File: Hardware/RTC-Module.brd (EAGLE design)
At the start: 25.4 x 25.4 mm, 18 parts, among them J4 455-1750-1-ND

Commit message: Board ready for design review
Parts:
- removed U$2: LOGO-SFESK, SparkFun:SFE-LOGO-FLAME
- added FD1, FD2, FD3, FD4: FIDUCIALUFIDUCIAL, SparkFun-Aesthetics:FIDUCIAL-MICRO
- added LOGO2: SFE_LOGO_FLAME.1_INCH, SparkFun-Aesthetics:SFE_LOGO_FLAME_.1
- added LOGO3: SFE_LOGO_NAME_FLAME.1_INCH, SparkFun-Aesthetics:SFE_LOGO_NAME_FLAME_.1
- BAT1: device SparkFun-Electromechanical:BATTCON_12MM_PTH -> SparkFun-Batteries:BATTCON_12MM_PTH
- moved FRAME2 67.9 mm to (-12.7, -8.89)
- moved LOGO1 37.9 mm to (2.54, 18.2)
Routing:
- net SDA: track 22.6 -> 48.6 mm, vias 0 -> 2
- net SCL: track 17.3 -> 40.6 mm, vias 2 -> 3
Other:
- board text added: "Andy England"
- board text added: "v01"
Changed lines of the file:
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@@
 <text x="17.907" y="9.779" size="0.8128" layer="21" font="vector" ratio="15" rot="R180" align="center">I</text>
 <text x="16.383" y="9.779" size="0.8128" layer="21" font="vector" ratio="15" rot="R180" align="center">F</text>
+<text x="24.892" y="0.508" size="1.27" layer="16" font="vector" ratio="15" rot="MR0">v01</text>
+<text x="13.97" y="-8.89" size="1.778" layer="51">Andy England</text>
 </plain>
 <attributes>
@@
 </autorouter>
 <elements>
-<element name="BAT1" library="SparkFun-Electromechanical" package="BATTCON_12MM_PTH" value="" x="12.7" y="19.05"/>
+<element name="BAT1" library="SparkFun-Batteries" package="BATTCON_12MM_PTH" value="" x="12.7" y="19.05">
+<attribute name="SF_SKU" value="PRT-07948" x="12.7" y="19.05" size="1.778" layer="27" display="off"/>
+<attribute name="PROD_ID" value="BATT-08315" x="12.7" y="19.05" size="1.778" layer="27" display="off"/>
+</element>
 <element name="C1" library="SparkFun-Capacitors" package="0603-CAP" value="0.1uF" x="22.86" y="7.62" rot="R270">
 <attribute name="PROD_ID" value="CAP-00810" x="22.86" y="7.62" size="1.778" layer="27" rot="R270" display="off"/>
 </element>
-<element name="FRAME2" library="SparkFun-Aesthetics" package="CREATIVE_COMMONS" value="FRAME-LETTER" x="-76.2" y="15.24"/>
+<element name="FRAME2" library="SparkFun-Aesthetics" package="CREATIVE_COMMONS" value="FRAME-LETTER" x="-12.7" y="-8.89"/>
 <element name="J1" library="SparkFun-Connectors" package="1X04_1MM_RA" value="" x="5.08" y="12.7" rot="R270">
 <attribute name="PROD_ID" value="CONN-13694" x="5.08" y="12.7" size="1.778" layer="27" rot="R270" display="off"/>
@@
 <attribute name="PROD_ID" value="XXX-00000" x="15.24" y="1.27" size="1.778" layer="27" display="off"/>
 </element>
-<element name="LOGO1" library="SparkFun-Aesthetics" package="OSHW-LOGO-S" value="OSHW-LOGOS" x="-30.48" y="36.83"/>
+<element name="LOGO1" library="SparkFun-Aesthetics" package="OSHW-LOGO-S" value="OSHW-LOGOS" x="2.54" y="18.161"/>
 <element name="R1" library="SparkFun-Resistors" package="0603" value="4.7k" x="7.62" y="7.62" rot="R90">
 <attribute name="PROD_ID" value="RES-07857" x="7.62" y="7.62" size="1.778" layer="27" rot="R90" display="off"/>
@@
 <element name="SJ1" library="SparkFun-Passives" package="SJ_3_PASTE1&amp;2&amp;3" value="" x="17.145" y="11.43"/>
 <element name="SJ2" library="SparkFun-Passives" package="SJ_3_PASTE1&amp;2&amp;3" value="" x="8.255" y="11.43"/>
-<element name="U$2" library="SparkFun" package="SFE-LOGO-FLAME" value="LOGO-SFESK" x="-24.13" y="31.75"/>
 <element name="U$6" library="SparkFun" package="STAND-OFF" value="STAND-OFF" x="22.86" y="22.86" rot="R180"/>
 <element name="U$7" library="SparkFun" package="STAND-OFF" value="STAND-OFF" x="2.54" y="22.86" rot="R180"/>
+<element name="LOGO2" library="SparkFun-Aesthetics" package="SFE_LOGO_FLAME_.1" value="SFE_LOGO_FLAME.1_INCH" x="21.717" y="16.764"/>
+<element name="LOGO3" library="SparkFun-Aesthetics" package="SFE_LOGO_NAME_FLAME_.1" value="SFE_LOGO_NAME_FLAME.1_INCH" x="18.669" y="13.843" rot="MR0"/>
+<element name="FD1" library="SparkFun-Aesthetics" package="FIDUCIAL-MICRO" value="FIDUCIALUFIDUCIAL" x="24.13" y="17.78" rot="MR0"/>
+<element name="FD2" library="SparkFun-Aesthetics" package="FIDUCIAL-MICRO" value="FIDUCIALUFIDUCIAL" x="24.13" y="17.78"/>
+<element name="FD3" library="SparkFun-Aesthetics" package="FIDUCIAL-MICRO" value="FIDUCIALUFIDUCIAL" x="1.27" y="1.27" rot="MR0"/>
+<element name="FD4" library="SparkFun-Aesthetics" package="FIDUCIAL-MICRO" value="FIDUCIALUFIDUCIAL" x="1.27" y="1.27"/>
 </elements>
 <signals>
@@
 <via x="19.05" y="10.668" extent="1-16" drill="0.381"/>
 <via x="22.86" y="5.588" extent="1-16" drill="0.381"/>
+<via x="16.129" y="8.763" extent="1-16" drill="0.381"/>
+<via x="16.51" y="4.064" extent="1-16" drill="0.381"/>
+<via x="19.05" y="5.334" extent="1-16" drill="0.381"/>
+<via x="13.97" y="2.667" extent="1-16" drill="0.381"/>
 </signal>
 <signal name="SCL">
@@
 <wire x1="3.81" y1="10.795" x2="4.215" y2="11.2" width="0.2032" layer="1"/>
 <wire x1="4.215" y1="11.2" x2="5.08" y2="11.2" width="0.2032" layer="1"/>
-<wire x1="11.43" y1="3.81" x2="20.32" y2="14.2" width="0" layer="19" extent="1-1"/>
+<wire x1="12.7" y1="1.27" x2="12.7" y2="2.54" width="0.2032" layer="16"/>
+<wire x1="12.7" y1="2.54" x2="21.59" y2="11.43" width="0.2032" layer="16"/>
+<wire x1="21.59" y1="11.43" x2="22.86" y2="11.43" width="0.2032" layer="16"/>
+<wire x1="22.86" y1="11.43" x2="24.13" y2="12.7" width="0.2032" layer="16"/>
+<wire x1="24.13" y1="12.7" x2="24.13" y2="13.97" width="0.2032" layer="16"/>
+<wire x1="24.13" y1="13.97" x2="22.86" y2="15.24" width="0.2032" layer="16"/>
+<wire x1="22.86" y1="15.24" x2="21.59" y2="15.24" width="0.2032" layer="16"/>
+<via x="21.59" y="15.24" extent="1-16" drill="0.381"/>
+<wire x1="21.59" y1="15.24" x2="20.828" y2="15.24" width="0.2032" layer="1"/>
+<wire x1="20.828" y1="15.24" x2="20.32" y2="14.732" width="0.2032" layer="1"/>
+<wire x1="20.32" y1="14.732" x2="20.32" y2="14.2" width="0.2032" layer="1"/>
 </signal>
 <signal name="SDA">
@@
 <wire x1="10.16" y1="1.27" x2="10.16" y2="2.54" width="0.2032" layer="1"/>
 <wire x1="10.16" y1="2.54" x2="9.398" y2="3.302" width="0.2032" layer="1"/>
-<wire x1="5.08" y1="12.2" x2="3.31" y2="12.2" width="0.2032" layer="1"/>
-<wire x1="3.31" y1="12.2" x2="2.921" y2="11.811" width="0.2032" layer="1"/>
-<wire x1="2.921" y1="11.811" x2="2.921" y2="4.191" width="0.2032" layer="1"/>
+<wire x1="5.08" y1="12.2" x2="2.921" y2="12.2" width="0.2032" layer="1"/>
+<wire x1="2.921" y1="12.2" x2="2.532" y2="12.2" width="0.2032" layer="1"/>
+<wire x1="2.921" y1="12.2" x2="2.921" y2="4.191" width="0.2032" layer="1"/>
 <wire x1="2.921" y1="4.191" x2="3.81" y2="3.302" width="0.2032" layer="1"/>
-<wire x1="5.08" y1="6.77" x2="5.08" y2="3.81" width="0.2032" layer="1"/>
+<wire x1="5.08" y1="6.77" x2="5.08" y2="3.302" width="0.2032" layer="1"/>
 <wire x1="5.08" y1="3.302" x2="3.81" y2="3.302" width="0.2032" layer="1"/>
 <wire x1="9.398" y1="3.302" x2="5.08" y2="3.302" width="0.2032" layer="1"/>
-<wire x1="5.08" y1="3.302" x2="5.08" y2="3.81" width="0.2032" layer="1"/>
-<wire x1="10.16" y1="2.54" x2="20.32" y2="13.2" width="0" layer="19" extent="1-1"/>
+<via x="2.032" y="12.7" extent="1-16" drill="0.381"/>
+<wire x1="2.032" y1="12.7" x2="2.532" y2="12.2" width="0.2032" layer="1"/>
+<wire x1="2.032" y1="12.7" x2="11.43" y2="12.7" width="0.2032" layer="16"/>
+<wire x1="11.43" y1="12.7" x2="12.7" y2="13.97" width="0.2032" layer="16"/>
+<wire x1="12.7" y1="13.97" x2="21.59" y2="13.97" width="0.2032" layer="16"/>
+<wire x1="20.32" y1="13.2" x2="22.36" y2="13.2" width="0.2032" layer="1"/>
+<wire x1="22.36" y1="13.2" x2="22.86" y2="12.7" width="0.2032" layer="1"/>
+<via x="22.86" y="12.7" extent="1-16" drill="0.381"/>
+<wire x1="22.86" y1="12.7" x2="21.59" y2="13.97" width="0.2032" layer="16"/>
 </signal>
 <signal name="N$5">

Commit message: post design review changes
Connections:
- net SCL: now also RTC1.8
- net SDA: now also RTC1.7
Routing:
- net SCL: track 40.6 -> 56.8 mm, vias 3 -> 4
- net SDA: track 48.6 -> 50.2 mm, vias 2 -> 3
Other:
- board text added: "0xD0"
- board text added: "32KHZ"
- board text added: "Qwiic RTC Module"
- board text added: "SQW/!INT"
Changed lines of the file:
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@@
 <layer number="45" name="Holes" color="7" fill="1" visible="no" active="yes"/>
 <layer number="46" name="Milling" color="3" fill="1" visible="no" active="yes"/>
-<layer number="47" name="Measures" color="7" fill="1" visible="no" active="yes"/>
+<layer number="47" name="Measures" color="7" fill="1" visible="yes" active="yes"/>
 <layer number="48" name="Document" color="7" fill="1" visible="yes" active="yes"/>
 <layer number="49" name="Reference" color="7" fill="1" visible="yes" active="yes"/>
@@
 <text x="12.7" y="3.937" size="0.8128" layer="22" font="vector" ratio="15" rot="MR270" align="center">SCL</text>
 <text x="15.24" y="3.937" size="0.8128" layer="22" font="vector" ratio="15" rot="MR270" align="center">!RST</text>
-<text x="17.78" y="3.937" size="0.8128" layer="22" font="vector" ratio="15" rot="MR270" align="center">!INT</text>
-<text x="20.32" y="3.937" size="0.8128" layer="22" font="vector" ratio="15" rot="MR270" align="center">32K</text>
+<text x="17.78" y="5.207" size="0.8128" layer="22" font="vector" ratio="15" rot="MR270" align="center">SQW/!INT</text>
+<text x="20.32" y="4.699" size="0.8128" layer="22" font="vector" ratio="15" rot="MR270" align="center">32KHZ</text>
 <text x="8.382" y="9.779" size="0.8128" layer="21" font="vector" ratio="15" rot="R180" align="center">I2C</text>
 <text x="17.907" y="9.779" size="0.8128" layer="21" font="vector" ratio="15" rot="R180" align="center">I</text>
 <text x="16.383" y="9.779" size="0.8128" layer="21" font="vector" ratio="15" rot="R180" align="center">F</text>
 <text x="24.892" y="0.508" size="1.27" layer="16" font="vector" ratio="15" rot="MR0">v01</text>
-<text x="13.97" y="-8.89" size="1.778" layer="51">Andy England</text>
+<text x="17.78" y="-8.89" size="1.778" layer="51">Andy England</text>
+<text x="12.7" y="10.795" size="1.27" layer="22" font="vector" ratio="15" rot="MR0" align="center">Qwiic RTC
+Module</text>
+<text x="12.7" y="7.62" size="1.016" layer="22" font="vector" ratio="15" rot="MR0" align="center">0xD0</text>
+<dimension x1="0" y1="25.4" x2="0" y2="0" x3="-7.62" y3="12.7" textsize="1.016" textratio="15" layer="47" unit="inch"/>
+<dimension x1="2.54" y1="22.86" x2="2.54" y2="0" x3="-3.81" y3="11.43" textsize="1.016" textratio="15" layer="47" unit="inch"/>
+<dimension x1="2.54" y1="22.86" x2="22.86" y2="22.86" x3="12.7" y3="26.67" textsize="1.016" textratio="15" layer="47" unit="inch"/>
+<dimension x1="25.4" y1="25.4" x2="0" y2="25.4" x3="12.7" y3="30.48" textsize="1.016" textratio="15" layer="47" unit="inch"/>
 </plain>
 <attributes>
@@
 <vertex x="25.4" y="0"/>
 </polygon>
-<via x="1.27" y="11.43" extent="1-16" drill="0.381"/>
+<via x="1.27" y="11.303" extent="1-16" drill="0.381"/>
 <via x="1.27" y="8.382" extent="1-16" drill="0.381"/>
 <via x="19.05" y="10.668" extent="1-16" drill="0.381"/>
@@
 <wire x1="20.828" y1="15.24" x2="20.32" y2="14.732" width="0.2032" layer="1"/>
 <wire x1="20.32" y1="14.732" x2="20.32" y2="14.2" width="0.2032" layer="1"/>
+<contactref element="RTC1" pad="8"/>
+<wire x1="10.795" y1="11.69" x2="10.795" y2="13.335" width="0.2032" layer="1"/>
+<wire x1="10.795" y1="13.335" x2="10.16" y2="13.97" width="0.2032" layer="1"/>
+<via x="10.16" y="13.97" extent="1-16" drill="0.381"/>
+<wire x1="10.16" y1="13.97" x2="1.778" y2="13.97" width="0.2032" layer="16"/>
+<wire x1="1.778" y1="13.97" x2="1.143" y2="13.335" width="0.2032" layer="16"/>
+<wire x1="1.143" y1="13.335" x2="1.143" y2="12.446" width="0.2032" layer="16"/>
+<wire x1="1.143" y1="12.446" x2="1.651" y2="11.938" width="0.2032" layer="16"/>
+<wire x1="1.651" y1="11.938" x2="2.286" y2="11.938" width="0.2032" layer="16"/>
+<wire x1="2.286" y1="11.938" x2="3.81" y2="10.414" width="0.2032" layer="16"/>
 </signal>
 <signal name="SDA">
@@
 <wire x1="2.032" y1="12.7" x2="2.532" y2="12.2" width="0.2032" layer="1"/>
 <wire x1="2.032" y1="12.7" x2="11.43" y2="12.7" width="0.2032" layer="16"/>
-<wire x1="11.43" y1="12.7" x2="12.7" y2="13.97" width="0.2032" layer="16"/>
+<wire x1="11.43" y1="12.7" x2="12.065" y2="13.335" width="0.2032" layer="16"/>
+<wire x1="12.065" y1="13.335" x2="12.7" y2="13.97" width="0.2032" layer="16"/>
 <wire x1="12.7" y1="13.97" x2="21.59" y2="13.97" width="0.2032" layer="16"/>
 <wire x1="20.32" y1="13.2" x2="22.36" y2="13.2" width="0.2032" layer="1"/>
@@
 <via x="22.86" y="12.7" extent="1-16" drill="0.381"/>
 <wire x1="22.86" y1="12.7" x2="21.59" y2="13.97" width="0.2032" layer="16"/>
+<contactref element="RTC1" pad="7"/>
+<wire x1="12.065" y1="11.69" x2="12.065" y2="13.335" width="0.2032" layer="1"/>
+<via x="12.065" y="13.335" extent="1-16" drill="0.381"/>
 </signal>
 <signal name="N$5">
@@
 </board>
 </drawing>
+<compatibility>
+<note version="6.3" minversion="6.2.2" severity="warning">
+Since Version 6.2.2 text objects can contain more than one line,
+which will not be processed correctly with this version.
+</note>
+</compatibility>
 </eagle>

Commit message: updated sensor
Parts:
- removed R4: 4.7k, SparkFun-Resistors:0603
- removed RTC1: DS3231M, SparkFun-Clocks:SO08
- removed SJ1: (no value), SparkFun-Passives:SJ_3_PASTE1&2&3
- added C2: 10nF, SparkFun-Capacitors:0603
- added D1: 0.5A/40V/420mV, SparkFun-DiscreteSemi:SOD-323
- added D2: 120mA/40V/370mV, SparkFun-DiscreteSemi:SOD-523
- added JP1: JUMPER-SMT_2_NC_PASTE_SILK, SparkFun-Jumpers:SMT-JUMPER_2_NC_PASTE_SILK
- added R5: 1k, SparkFun-Resistors:0603
- added U1: RV-4162-C7, SparkFun-Clocks:RV-4162-C7-SMT
- C1: value 0.1uF -> 1.0uF; device SparkFun-Capacitors:0603-CAP -> SparkFun-Capacitors:0603
- J3: device SparkFun-Connectors:1X04 -> SparkFun-Connectors:1X04_NO_SILK
- J4: value 455-1750-1-ND -> (none); device SparkFun-Connectors:1X03 -> SparkFun-Connectors:1X01_NO_SILK
- R1, R2, R3: device SparkFun-Resistors:0603 -> SparkFun-Resistors:0603@1
- moved C1 8.03 mm to (15.2, 5.08), turned to 0 degrees
- moved R3 2.74 mm to (17.8, 8.64)
- moved J4 2.54 mm to (17.8, 1.27)
- moved J3 2.54 mm to (7.62, 1.27)
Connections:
- removed net !INT/SQW: J4.2, R4.1, RTC1.3
- removed net !RST: J4.1, RTC1.4
- removed net 32KHZ: J4.3, R3.1, RTC1.1
- removed net N$1: BAT1.VCC@1, RTC1.6
- removed net N$3: R4.2, SJ1.1
- new net !INT: J4.1, R3.1, U1.6
- new net BATTERY: BAT1.VCC@1, C1.1, D2.A, R5.1
- new net CLKOUT: U1.2
- new net N$4: D1.C, R5.2
- net 3.3V: now also C2.1, D1.A, D2.C, JP1.2, U1.5; no longer C1.1, RTC1.2, SJ1.2
- net GND: now also C2.2, U1.3; no longer RTC1.5
- net N$2: now also JP1.1; no longer SJ1.3
- net SCL: now also U1.8; no longer RTC1.8
- net SDA: now also U1.1; no longer RTC1.7
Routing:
- net SCL: track 56.8 -> 0.00 mm, vias 4 -> 0
- net SDA: track 50.2 -> 0.00 mm, vias 3 -> 0
- net 3.3V: track 41.7 -> 4.65 mm, vias 3 -> 0
- net 32KHZ: track 16.8 -> 0.00 mm
- net N$1: track 12.1 -> 0.00 mm
- net !INT/SQW: track 11.0 -> 0.00 mm
- net BATTERY: track 0.00 -> 10.4 mm
- net !RST: track 5.08 -> 0.00 mm
- net N$2: track 4.83 -> 0.00 mm
- net N$3: track 4.08 -> 0.00 mm
- net N$5: track 6.03 -> 3.93 mm
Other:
- board text removed: "!INT"
- board text removed: "!RST"
- board text removed: "0xD0"
- board text removed: "3.3V"
- board text removed: "32K"
- board text removed: "32KHZ"
- board text removed: "F"
- board text removed: "GND"
- board text removed: "I"
- board text removed: "SCL"
- board text removed: "SDA"
- board text removed: "SQW/!INT"

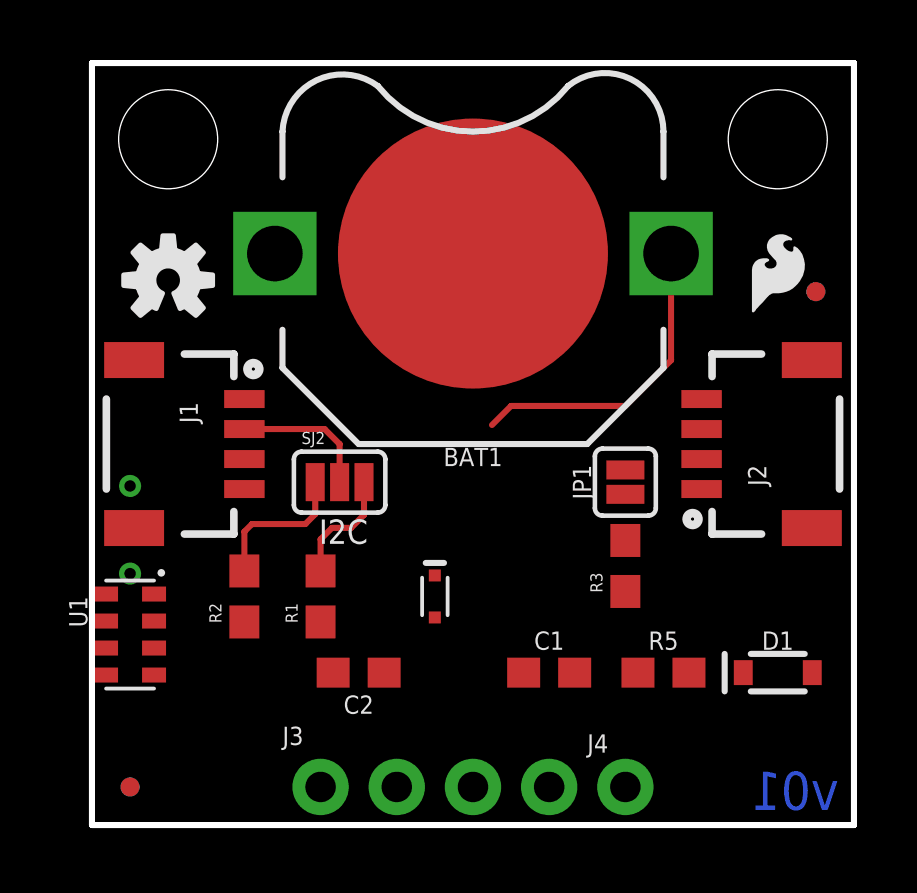
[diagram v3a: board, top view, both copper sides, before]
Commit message: Updated RTC module
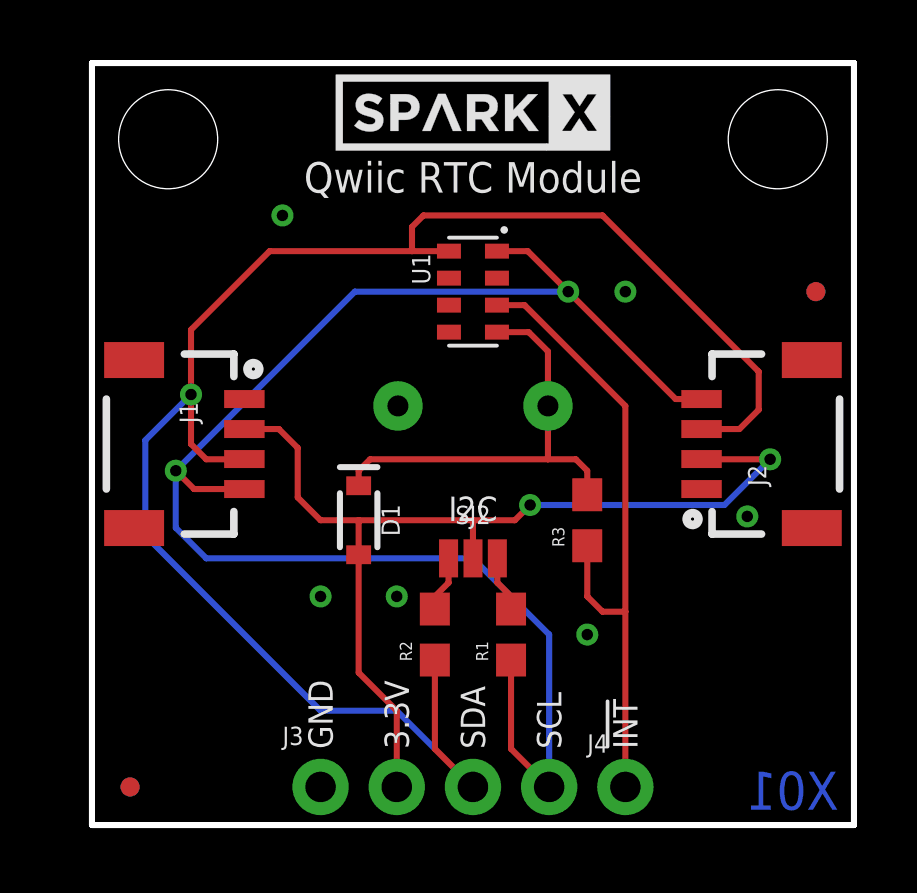
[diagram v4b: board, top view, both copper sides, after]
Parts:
- removed BAT1: (no value), SparkFun-Batteries:BATTCON_12MM_PTH
- removed C2: 10nF, SparkFun-Capacitors:0603
- removed D2: 120mA/40V/370mV, SparkFun-DiscreteSemi:SOD-523
- removed JP1: JUMPER-SMT_2_NC_PASTE_SILK, SparkFun-Jumpers:SMT-JUMPER_2_NC_PASTE_SILK
- removed LOGO2: SFE_LOGO_FLAME.1_INCH, SparkFun-Aesthetics:SFE_LOGO_FLAME_.1
- removed LOGO3: SFE_LOGO_NAME_FLAME.1_INCH, SparkFun-Aesthetics:SFE_LOGO_NAME_FLAME_.1
- removed R5: 1k, SparkFun-Resistors:0603
- added U$3: SPARKX-LOGO2, SparkX:SPARKX-TINY
- added U$5: SPARKX-LOGO4, SparkX:SPARKX-MEDIUM
- C1: value 1.0uF -> 1F-EDLC; device SparkFun-Capacitors:0603 -> SparkFun-Capacitors:CAP-RADIAL-5MM-21.5MM
- SJ2: value (none) -> JUMPER-SMT_3_2-NC_PASTE_NO-SILK; device SparkFun-Passives:SJ_3_PASTE1&2&3 -> SparkFun-Jumpers:SMT-JUMPER_3_2-NC_PASTE_NO-SILK
- moved LOGO1 16.6 mm to (3.81, 1.65), flipped to the bottom
- moved U1 16.2 mm to (12.7, 17.8)
- moved D1 14.9 mm to (8.89, 10.2), turned to 270 degrees
- moved C1 9.25 mm to (12.7, 14.0), flipped to the bottom
- moved R1 6.48 mm to (14.0, 6.35)
- moved R2 6.48 mm to (11.4, 6.35)
- moved SJ2 5.12 mm to (12.7, 8.89)
- moved R3 1.98 mm to (16.5, 10.2)
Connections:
- removed net BATTERY: BAT1.VCC@1, C1.1, D2.A, R5.1
- removed net N$2 (its old number): JP1.1, R3.2
- removed net N$4: D1.C, R5.2
- new net VBATT: C1.+, D1.C, R3.2, U1.5
- net 3.3V: no longer C2.1, D2.C, JP1.2, U1.5
- net GND: now also C1.-; no longer BAT1.GND, C1.2, C2.2
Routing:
- net SDA: track 0.00 -> 58.1 mm, vias 0 -> 1
- net SCL: track 0.00 -> 52.6 mm, vias 0 -> 2
- net 3.3V: track 4.65 -> 33.6 mm, vias 0 -> 2
- net !INT: track 0.00 -> 21.5 mm
- net VBATT: track 0.00 -> 14.8 mm
- net BATTERY: track 10.4 -> 0.00 mm
- net N$2: track 4.98 -> 1.88 mm
- net N$1: track 3.93 -> 1.88 mm
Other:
- board text added: "!INT"
- board text added: "3.3V"
- board text added: "GND"
- board text added: "SCL"
- board text added: "SDA"
- board text added: "X01"
- board text removed: "v01"
